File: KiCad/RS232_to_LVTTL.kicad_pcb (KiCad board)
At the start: 2 copper layers, 36.1 x 34 mm, 19 parts, among them J1 DB25_Female, J2 Conn_01x05, U1 TPS54308, U2 MAX3232

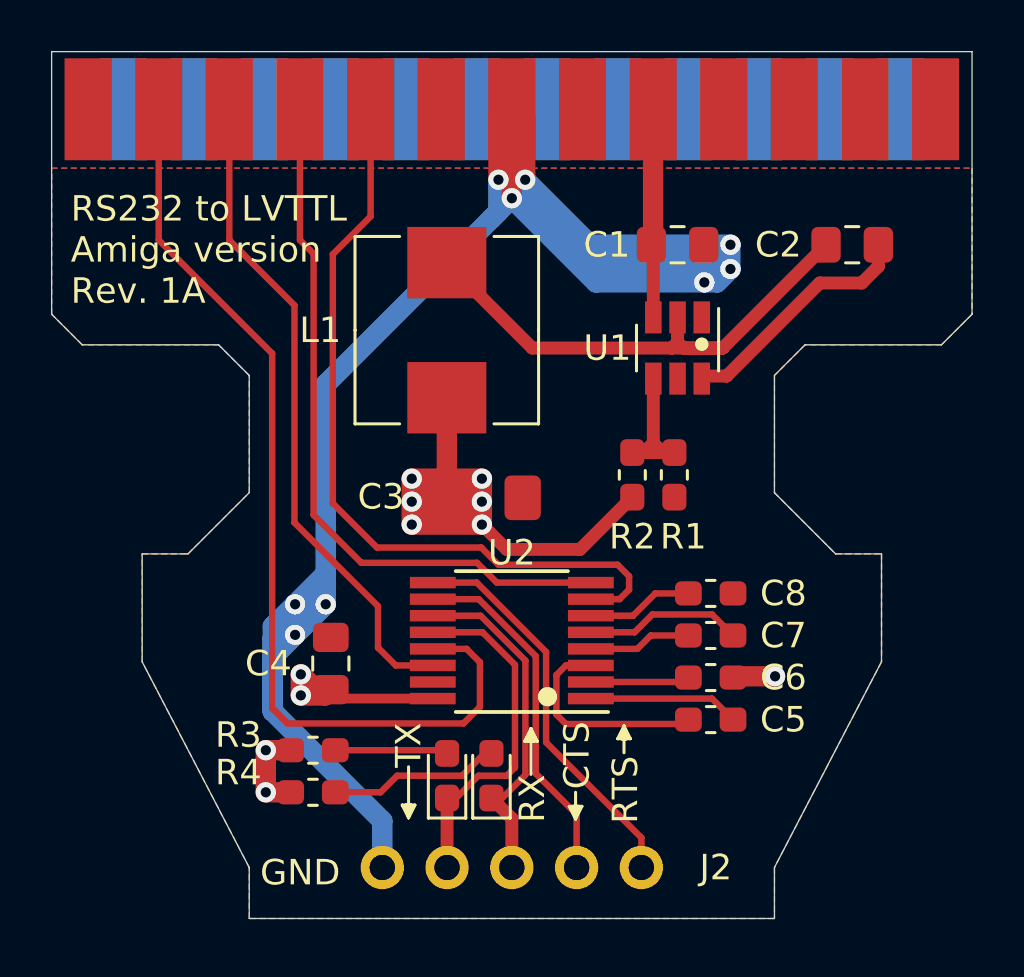
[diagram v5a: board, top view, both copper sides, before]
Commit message: Added a PWR LED and some final routing and silkscreen fixes
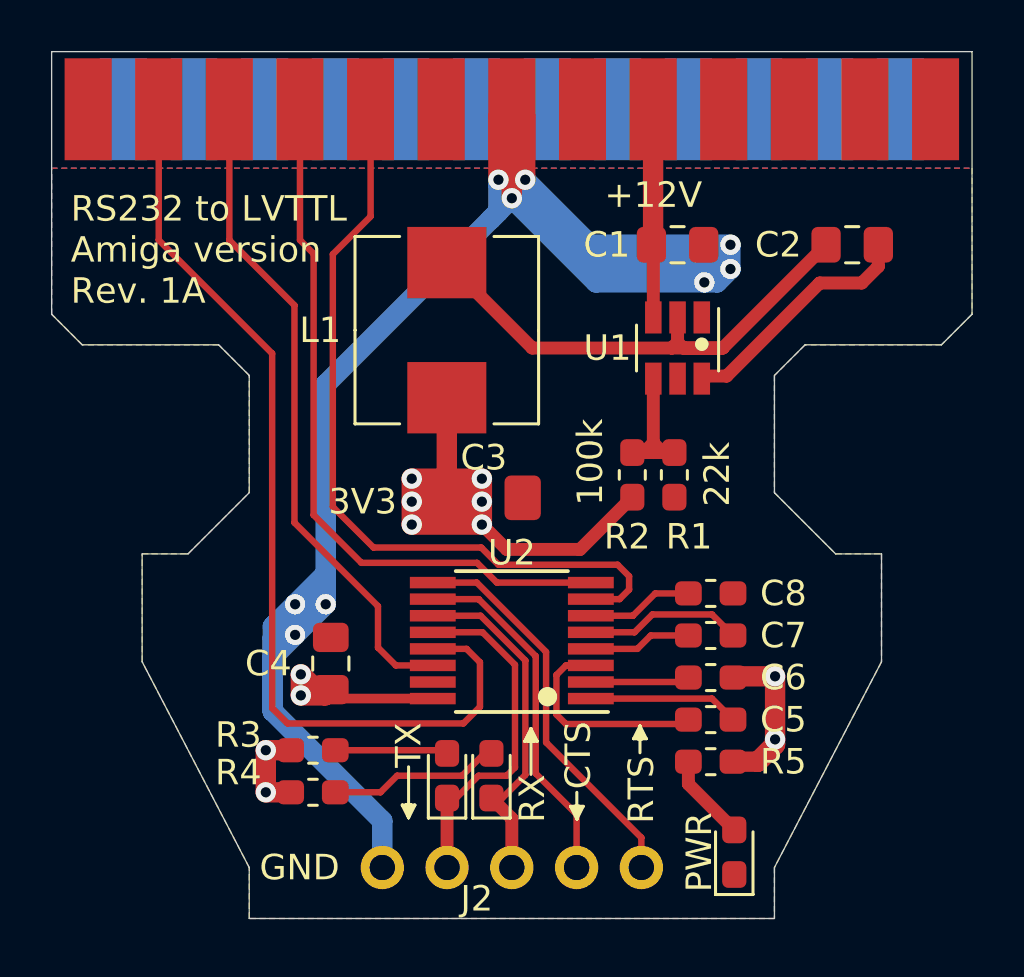
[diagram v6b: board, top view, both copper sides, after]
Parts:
- added D3: LED, Diode_SMD:D_0603_1608Metric_Pad1.05x0.95mm_HandSolder, F.Cu at (115.2, 81.4)
- added R5: 1k, Resistor_SMD:R_0603_1608Metric_Pad1.05x0.95mm_HandSolder, F.Cu at (114.3, 77.8)
- added REF**: OSHW-Logo_11.4x12mm_SilkScreen, Symbol:OSHW-Logo_11.4x12mm_SilkScreen, B.Cu at (109.7, 72.3)
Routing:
- net 3V3: track 41.1 -> 45.7 mm, vias 11 -> 12
- net Net-(D3-Pad2): track 0.00 -> 3.42 mm
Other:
- board text added: "+12V"
- board text added: "100k"
- board text added: "22k"
- board text added: "3V3"
- board text added: "PWR"

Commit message: some small routing and silkscreen fixes
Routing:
- net GND: track 91.4 -> 113.5 mm, vias 9 -> 11
- net CTS: track 31.5 -> 30.9 mm

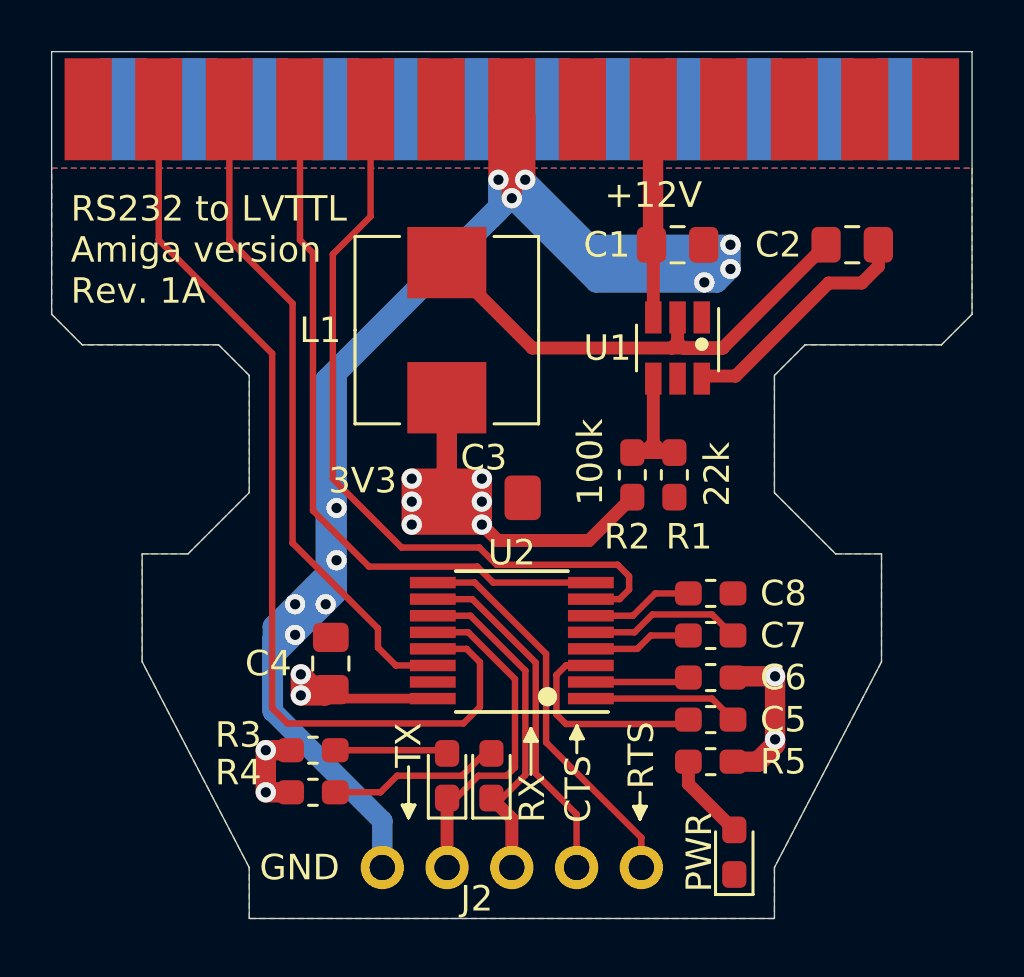
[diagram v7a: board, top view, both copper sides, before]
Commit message: Moved the Inductor a little to the right to get further away from the signal traces
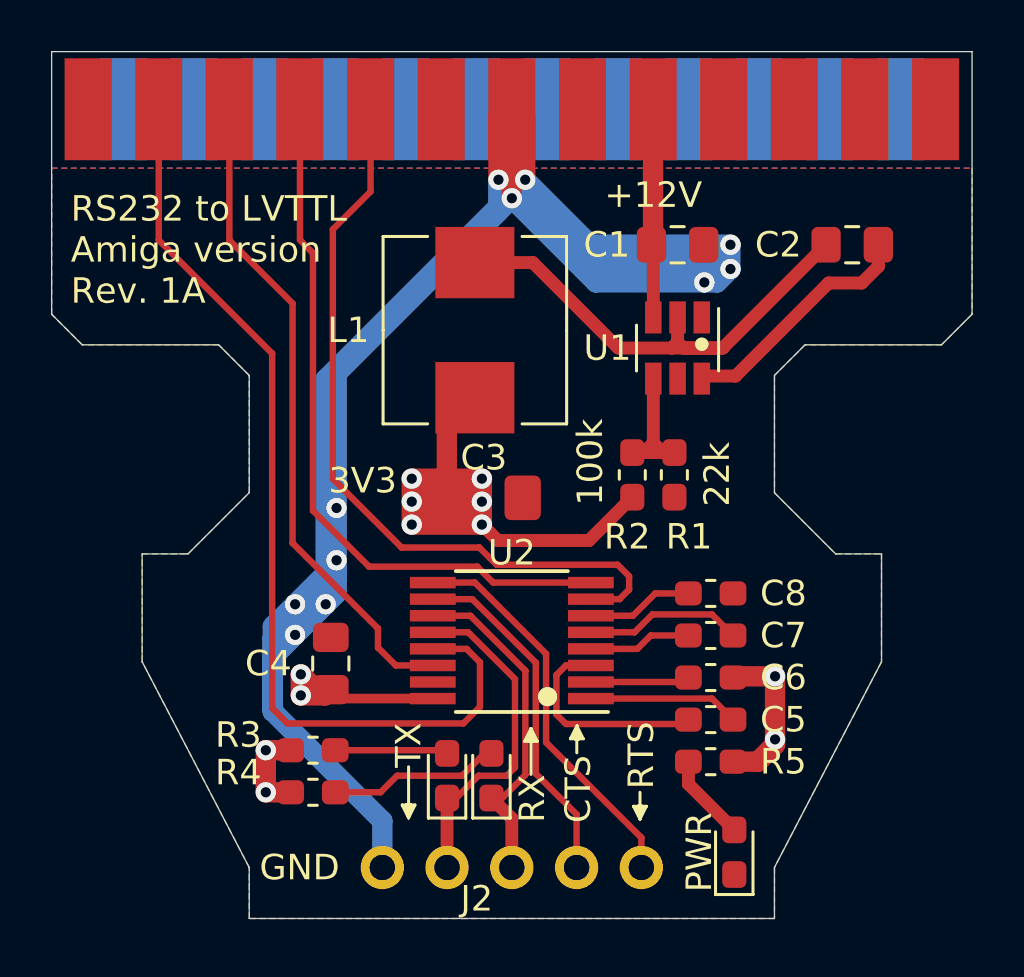
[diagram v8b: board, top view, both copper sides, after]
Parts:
- moved L1 1.10 mm to (105.0, 60.9)
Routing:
- net Net-(C2-Pad2): track 21.0 -> 19.9 mm
